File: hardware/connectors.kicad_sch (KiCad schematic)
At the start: 9 parts, among them J1 Signals, J2 Diagnostics, J3 Power & CAN

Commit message: Refactor
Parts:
- J1: symbol conn_02x20_odd_even:Conn_02x20_Odd_Even -> Connector_Generic:Conn_02x20_Odd_Even
- J2, J3: symbol conn_02x10_odd_even:Conn_02x10_Odd_Even -> Connector_Generic:Conn_02x10_Odd_Even
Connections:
- net CAN-H renamed CAN+
- net CAN-L renamed CAN-
- net SAFETY-IN renamed SAFETY_IN
- net SAFETY-OUT renamed SAFETY_OUT
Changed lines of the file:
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@@
     (effects (font (size 1.27 1.27)) (justify left bottom))
   )
-  (global_label "SAFETY-OUT" (shape input) (at 72.39 87.63 180) (fields_autoplaced)
-    (effects (font (size 1.27 1.27)) (justify right))
-    (property "Intersheetrefs" "${INTERSHEET_REFS}" (at 58.2729 87.5506 0)
+  (global_label "SAFETY_OUT" (shape input) (at 72.39 87.63 180) (fields_autoplaced)
+    (effects (font (size 1.27 1.27)) (justify right))
+    (property "Intersheetrefs" "${INTERSHEET_REFS}" (at 58.9503 87.63 0)
       (effects (font (size 1.27 1.27)) (justify right) hide)
     )
@@
     )
   )
-  (global_label "SAFETY-IN" (shape output) (at 72.39 85.09 180) (fields_autoplaced)
-    (effects (font (size 1.27 1.27)) (justify right))
-    (property "Intersheetrefs" "${INTERSHEET_REFS}" (at 60.0388 85.09 0)
-      (effects (font (size 1.27 1.27)) (justify right) hide)
-    )
-  )
-  (global_label "CAN-L" (shape input) (at 213.36 96.52 180) (fields_autoplaced)
-    (effects (font (size 1.27 1.27)) (justify right))
-    (property "Intersheetrefs" "${INTERSHEET_REFS}" (at 204.7463 96.4406 0)
+  (global_label "SAFETY_IN" (shape output) (at 72.39 85.09 180) (fields_autoplaced)
+    (effects (font (size 1.27 1.27)) (justify right))
+    (property "Intersheetrefs" "${INTERSHEET_REFS}" (at 60.6436 85.09 0)
+      (effects (font (size 1.27 1.27)) (justify right) hide)
+    )
+  )
+  (global_label "CAN-" (shape input) (at 213.36 96.52 180) (fields_autoplaced)
+    (effects (font (size 1.27 1.27)) (justify right))
+    (property "Intersheetrefs" "${INTERSHEET_REFS}" (at 205.8469 96.52 0)
       (effects (font (size 1.27 1.27)) (justify right) hide)
     )
@@
     )
   )
-  (global_label "CAN-H" (shape input) (at 213.36 93.98 180) (fields_autoplaced)
-    (effects (font (size 1.27 1.27)) (justify right))
-    (property "Intersheetrefs" "${INTERSHEET_REFS}" (at 204.4439 93.9006 0)
+  (global_label "CAN+" (shape input) (at 213.36 93.98 180) (fields_autoplaced)
+    (effects (font (size 1.27 1.27)) (justify right))
+    (property "Intersheetrefs" "${INTERSHEET_REFS}" (at 205.8469 93.98 0)
       (effects (font (size 1.27 1.27)) (justify right) hide)
     )
@@
     (pin "2")
     (instances
-      (project "APPS"
+      (project "apps"
         (path "/fc4ad874-c922-4070-89f9-7262080469d8/00000000-0000-0000-0000-00006077b773"
           (reference "R33") (unit 1)
@@
     (pin "2")
     (instances
-      (project "APPS"
+      (project "apps"
         (path "/fc4ad874-c922-4070-89f9-7262080469d8/00000000-0000-0000-0000-00006077b773"
           (reference "R43") (unit 1)
@@
     (pin "1")
     (instances
-      (project "APPS"
+      (project "apps"
         (path "/fc4ad874-c922-4070-89f9-7262080469d8/00000000-0000-0000-0000-00006077b773"
           (reference "#PWR048") (unit 1)
@@
     (pin "1")
     (instances
-      (project "APPS"
+      (project "apps"
         (path "/fc4ad874-c922-4070-89f9-7262080469d8/00000000-0000-0000-0000-00006077b773"
           (reference "#PWR047") (unit 1)
@@
     (pin "2")
     (instances
-      (project "APPS"
+      (project "apps"
         (path "/fc4ad874-c922-4070-89f9-7262080469d8/00000000-0000-0000-0000-00006077b773"
           (reference "R42") (unit 1)
@@
     (pin "1")
     (instances
-      (project "APPS"
+      (project "apps"
         (path "/fc4ad874-c922-4070-89f9-7262080469d8/00000000-0000-0000-0000-00006077b773"
           (reference "#PWR045") (unit 1)
@@
     )
   )
-  (symbol (lib_id "conn_02x10_odd_even:Conn_02x10_Odd_Even") (at 133.35 101.6 0) (unit 1)
+  (symbol (lib_id "Connector_Generic:Conn_02x10_Odd_Even") (at 135.89 101.6 0) (mirror y) (unit 1)
     (in_bom yes) (on_board yes) (dnp no)
     (property "Reference" "J2" (at 134.62 85.9282 0)
@@
       (effects (font (size 1.27 1.27)))
     )
-    (property "Footprint" "Connector_PinSocket_2.54mm:PinSocket_2x10_P2.54mm_Vertical" (at 133.35 101.6 0)
-      (effects (font (size 1.27 1.27)) hide)
-    )
-    (property "Datasheet" "~" (at 133.35 101.6 0)
+    (property "Footprint" "Connector_PinSocket_2.54mm:PinSocket_2x10_P2.54mm_Vertical" (at 135.89 101.6 0)
+      (effects (font (size 1.27 1.27)) hide)
+    )
+    (property "Datasheet" "~" (at 135.89 101.6 0)
       (effects (font (size 1.27 1.27)) hide)
     )
@@
     (pin "9")
     (instances
-      (project "APPS"
+      (project "apps"
         (path "/fc4ad874-c922-4070-89f9-7262080469d8/00000000-0000-0000-0000-00006077b773"
           (reference "J2") (unit 1)
@@
     (pin "1")
     (instances
-      (project "APPS"
+      (project "apps"
         (path "/fc4ad874-c922-4070-89f9-7262080469d8/00000000-0000-0000-0000-00006077b773"
           (reference "#PWR043") (unit 1)
@@
     (pin "1")
     (instances
-      (project "APPS"
+      (project "apps"
         (path "/fc4ad874-c922-4070-89f9-7262080469d8/00000000-0000-0000-0000-00006077b773"
           (reference "#PWR044") (unit 1)
@@
     (pin "1")
     (instances
-      (project "APPS"
+      (project "apps"
         (path "/fc4ad874-c922-4070-89f9-7262080469d8/00000000-0000-0000-0000-00005f60f83f"
           (reference "#PWR019") (unit 1)
@@
     (pin "1")
     (instances
-      (project "APPS"
+      (project "apps"
         (path "/fc4ad874-c922-4070-89f9-7262080469d8/00000000-0000-0000-0000-00006077b773"
           (reference "#PWR046") (unit 1)
@@
     )
   )
-  (symbol (lib_id "conn_02x10_odd_even:Conn_02x10_Odd_Even") (at 224.79 99.06 0) (unit 1)
+  (symbol (lib_id "Connector_Generic:Conn_02x10_Odd_Even") (at 227.33 99.06 0) (mirror y) (unit 1)
     (in_bom yes) (on_board yes) (dnp no)
     (property "Reference" "J3" (at 226.06 83.3882 0)
@@
       (effects (font (size 1.27 1.27)))
     )
-    (property "Footprint" "Connector_PinSocket_2.54mm:PinSocket_2x10_P2.54mm_Vertical" (at 224.79 99.06 0)
-      (effects (font (size 1.27 1.27)) hide)
-    )
-    (property "Datasheet" "~" (at 224.79 99.06 0)
+    (property "Footprint" "Connector_PinSocket_2.54mm:PinSocket_2x10_P2.54mm_Vertical" (at 227.33 99.06 0)
+      (effects (font (size 1.27 1.27)) hide)
+    )
+    (property "Datasheet" "~" (at 227.33 99.06 0)
       (effects (font (size 1.27 1.27)) hide)
     )
@@
     (pin "9")
     (instances
-      (project "APPS"
+      (project "apps"
         (path "/fc4ad874-c922-4070-89f9-7262080469d8/00000000-0000-0000-0000-00006077b773"
           (reference "J3") (unit 1)
@@
     (pin "1")
     (instances
-      (project "APPS"
+      (project "apps"
         (path "/fc4ad874-c922-4070-89f9-7262080469d8/00000000-0000-0000-0000-00006077b773"
           (reference "#FLG02") (unit 1)
@@
     (pin "1")
     (instances
-      (project "APPS"
+      (project "apps"
         (path "/fc4ad874-c922-4070-89f9-7262080469d8/00000000-0000-0000-0000-00006077b773"
           (reference "#FLG04") (unit 1)
@@
     )
   )
-  (symbol (lib_id "conn_02x20_odd_even:Conn_02x20_Odd_Even") (at 80.01 100.33 0) (unit 1)
+  (symbol (lib_id "Connector_Generic:Conn_02x20_Odd_Even") (at 82.55 100.33 0) (mirror y) (unit 1)
     (in_bom yes) (on_board yes) (dnp no)
     (property "Reference" "J1" (at 81.28 71.9582 0)
@@
       (effects (font (size 1.27 1.27)))
     )
-    (property "Footprint" "Connector_PinSocket_2.54mm:PinSocket_2x20_P2.54mm_Vertical" (at 80.01 100.33 0)
-      (effects (font (size 1.27 1.27)) hide)
-    )
-    (property "Datasheet" "~" (at 80.01 100.33 0)
+    (property "Footprint" "Connector_PinSocket_2.54mm:PinSocket_2x20_P2.54mm_Vertical" (at 82.55 100.33 0)
+      (effects (font (size 1.27 1.27)) hide)
+    )
+    (property "Datasheet" "~" (at 82.55 100.33 0)
       (effects (font (size 1.27 1.27)) hide)
     )
@@
     (pin "9")
     (instances
-      (project "APPS"
+      (project "apps"
         (path "/fc4ad874-c922-4070-89f9-7262080469d8/00000000-0000-0000-0000-00006077b773"
           (reference "J1") (unit 1)
@@
     (pin "1")
     (instances
-      (project "APPS"
+      (project "apps"
         (path "/fc4ad874-c922-4070-89f9-7262080469d8/00000000-0000-0000-0000-00006077b773"
           (reference "#PWR042") (unit 1)
@@
     (pin "2")
     (instances
-      (project "APPS"
+      (project "apps"
         (path "/fc4ad874-c922-4070-89f9-7262080469d8/00000000-0000-0000-0000-00006077b773"
           (reference "R30") (unit 1)
@@
     (pin "2")
     (instances
-      (project "APPS"
+      (project "apps"
         (path "/fc4ad874-c922-4070-89f9-7262080469d8/00000000-0000-0000-0000-00006077b773"
           (reference "R32") (unit 1)
@@
     (pin "2")
     (instances
-      (project "APPS"
+      (project "apps"
         (path "/fc4ad874-c922-4070-89f9-7262080469d8/00000000-0000-0000-0000-00006077b773"
           (reference "R31") (unit 1)
@@
     (pin "1")
     (instances
-      (project "APPS"
+      (project "apps"
         (path "/fc4ad874-c922-4070-89f9-7262080469d8/00000000-0000-0000-0000-00006077b773"
           (reference "#FLG03") (unit 1)

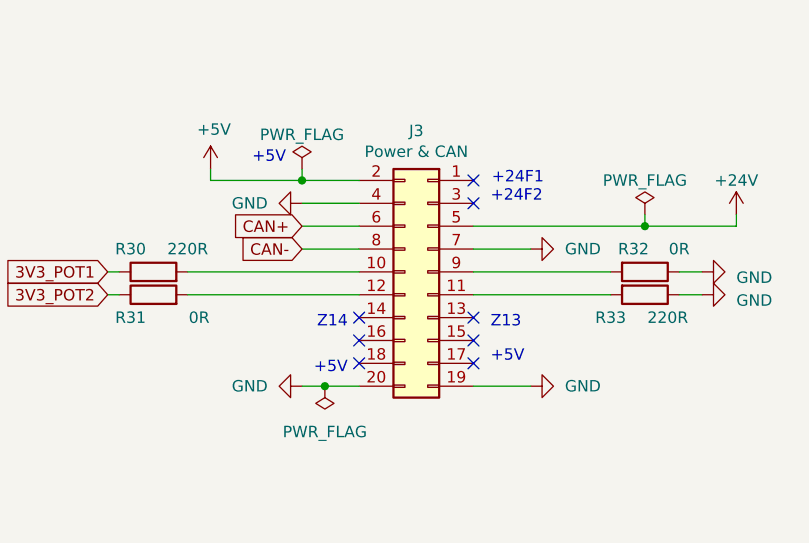
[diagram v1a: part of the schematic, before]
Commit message: Adjust component values
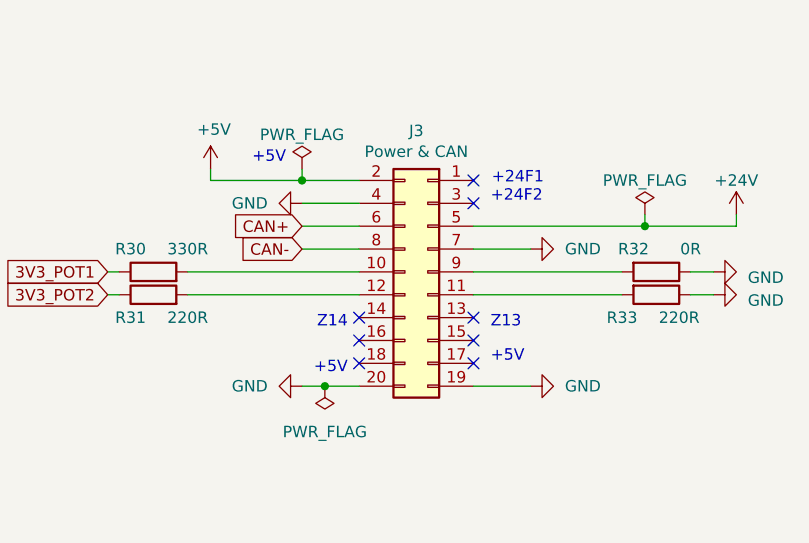
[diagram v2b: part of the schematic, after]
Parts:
- R30: value 220R -> 330R
- R31: value 0R -> 220R
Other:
- moved on the sheet: R32, R33
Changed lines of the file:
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@@
   (title_block
     (title "Connectors")
-    (date "2023-04-22")
+    (date "2023-06-30")
     (rev "2.0")
     (company "S. Sambor")
@@
     (stroke (width 0) (type default))
   )
-  (wire (pts (xy 232.41 99.06) (xy 247.65 99.06))
-    (stroke (width 0) (type default))
-  )
-  (wire (pts (xy 255.27 99.06) (xy 257.81 99.06))
+  (wire (pts (xy 232.41 99.06) (xy 248.92 99.06))
+    (stroke (width 0) (type default))
+  )
+  (wire (pts (xy 256.54 99.06) (xy 259.08 99.06))
     (stroke (width 0) (type default))
   )
@@
     (stroke (width 0) (type default))
   )
-  (wire (pts (xy 255.27 101.6) (xy 257.81 101.6))
+  (wire (pts (xy 256.54 101.6) (xy 259.08 101.6))
     (stroke (width 0) (type default))
   )
@@
     (stroke (width 0) (type default))
   )
-  (wire (pts (xy 232.41 101.6) (xy 247.65 101.6))
+  (wire (pts (xy 232.41 101.6) (xy 248.92 101.6))
     (stroke (width 0) (type default))
   )
@@
     )
   )
-  (symbol (lib_id "Device:R") (at 251.46 101.6 270) (unit 1)
-    (in_bom yes) (on_board yes) (dnp no)
-    (property "Reference" "R33" (at 247.65 104.14 90)
-      (effects (font (size 1.27 1.27)))
-    )
-    (property "Value" "220R" (at 254 104.14 90)
-      (effects (font (size 1.27 1.27)))
-    )
-    (property "Footprint" "Resistor_SMD:R_0603_1608Metric_Pad0.98x0.95mm_HandSolder" (at 251.46 99.822 90)
-      (effects (font (size 1.27 1.27)) hide)
-    )
-    (property "Datasheet" "~" (at 251.46 101.6 0)
+  (symbol (lib_id "Device:R") (at 252.73 101.6 270) (unit 1)
+    (in_bom yes) (on_board yes) (dnp no)
+    (property "Reference" "R33" (at 248.92 104.14 90)
+      (effects (font (size 1.27 1.27)))
+    )
+    (property "Value" "220R" (at 255.27 104.14 90)
+      (effects (font (size 1.27 1.27)))
+    )
+    (property "Footprint" "Resistor_SMD:R_0603_1608Metric_Pad0.98x0.95mm_HandSolder" (at 252.73 99.822 90)
+      (effects (font (size 1.27 1.27)) hide)
+    )
+    (property "Datasheet" "~" (at 252.73 101.6 0)
       (effects (font (size 1.27 1.27)) hide)
     )
@@
     )
   )
-  (symbol (lib_id "power:GND") (at 257.81 101.6 90) (unit 1)
+  (symbol (lib_id "power:GND") (at 259.08 101.6 90) (unit 1)
     (in_bom yes) (on_board yes) (dnp no) (fields_autoplaced)
-    (property "Reference" "#PWR047" (at 264.16 101.6 0)
-      (effects (font (size 1.27 1.27)) hide)
-    )
-    (property "Value" "GND" (at 261.62 102.235 90)
+    (property "Reference" "#PWR047" (at 265.43 101.6 0)
+      (effects (font (size 1.27 1.27)) hide)
+    )
+    (property "Value" "GND" (at 262.89 102.235 90)
       (effects (font (size 1.27 1.27)) (justify right))
     )
-    (property "Footprint" "" (at 257.81 101.6 0)
-      (effects (font (size 1.27 1.27)) hide)
-    )
-    (property "Datasheet" "" (at 257.81 101.6 0)
+    (property "Footprint" "" (at 259.08 101.6 0)
+      (effects (font (size 1.27 1.27)) hide)
+    )
+    (property "Datasheet" "" (at 259.08 101.6 0)
       (effects (font (size 1.27 1.27)) hide)
     )
@@
     )
   )
-  (symbol (lib_id "power:GND") (at 257.81 99.06 90) (unit 1)
+  (symbol (lib_id "power:GND") (at 259.08 99.06 90) (unit 1)
     (in_bom yes) (on_board yes) (dnp no) (fields_autoplaced)
-    (property "Reference" "#PWR046" (at 264.16 99.06 0)
-      (effects (font (size 1.27 1.27)) hide)
-    )
-    (property "Value" "GND" (at 261.62 99.695 90)
+    (property "Reference" "#PWR046" (at 265.43 99.06 0)
+      (effects (font (size 1.27 1.27)) hide)
+    )
+    (property "Value" "GND" (at 262.89 99.695 90)
       (effects (font (size 1.27 1.27)) (justify right))
     )
-    (property "Footprint" "" (at 257.81 99.06 0)
-      (effects (font (size 1.27 1.27)) hide)
-    )
-    (property "Datasheet" "" (at 257.81 99.06 0)
+    (property "Footprint" "" (at 259.08 99.06 0)
+      (effects (font (size 1.27 1.27)) hide)
+    )
+    (property "Datasheet" "" (at 259.08 99.06 0)
       (effects (font (size 1.27 1.27)) hide)
     )
@@
       (effects (font (size 1.27 1.27)))
     )
-    (property "Value" "220R" (at 200.66 96.52 90)
+    (property "Value" "330R" (at 200.66 96.52 90)
       (effects (font (size 1.27 1.27)))
     )
@@
     )
   )
-  (symbol (lib_id "Device:R") (at 251.46 99.06 270) (unit 1)
+  (symbol (lib_id "Device:R") (at 252.73 99.06 270) (unit 1)
     (in_bom yes) (on_board yes) (dnp no)
     (property "Reference" "R32" (at 250.19 96.52 90)
       (effects (font (size 1.27 1.27)))
     )
-    (property "Value" "0R" (at 255.27 96.52 90)
-      (effects (font (size 1.27 1.27)))
-    )
-    (property "Footprint" "Resistor_SMD:R_0603_1608Metric_Pad0.98x0.95mm_HandSolder" (at 251.46 97.282 90)
-      (effects (font (size 1.27 1.27)) hide)
-    )
-    (property "Datasheet" "~" (at 251.46 99.06 0)
+    (property "Value" "0R" (at 256.54 96.52 90)
+      (effects (font (size 1.27 1.27)))
+    )
+    (property "Footprint" "Resistor_SMD:R_0603_1608Metric_Pad0.98x0.95mm_HandSolder" (at 252.73 97.282 90)
+      (effects (font (size 1.27 1.27)) hide)
+    )
+    (property "Datasheet" "~" (at 252.73 99.06 0)
       (effects (font (size 1.27 1.27)) hide)
     )
@@
       (effects (font (size 1.27 1.27)))
     )
-    (property "Value" "0R" (at 201.93 104.14 90)
-      (effects (font (size 1.27 1.27)))
-    )
+    (property "Value" "220R" (at 200.66 104.14 90)
+      (effects (font (size 1.27 1.27)))
+    )
